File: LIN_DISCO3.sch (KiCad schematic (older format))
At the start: 18 parts, among them J1 Conn_01x06_Female, U1 PIC16F628-xxISO, U2 MCP1804x-5002xMB, U3 Si9243A

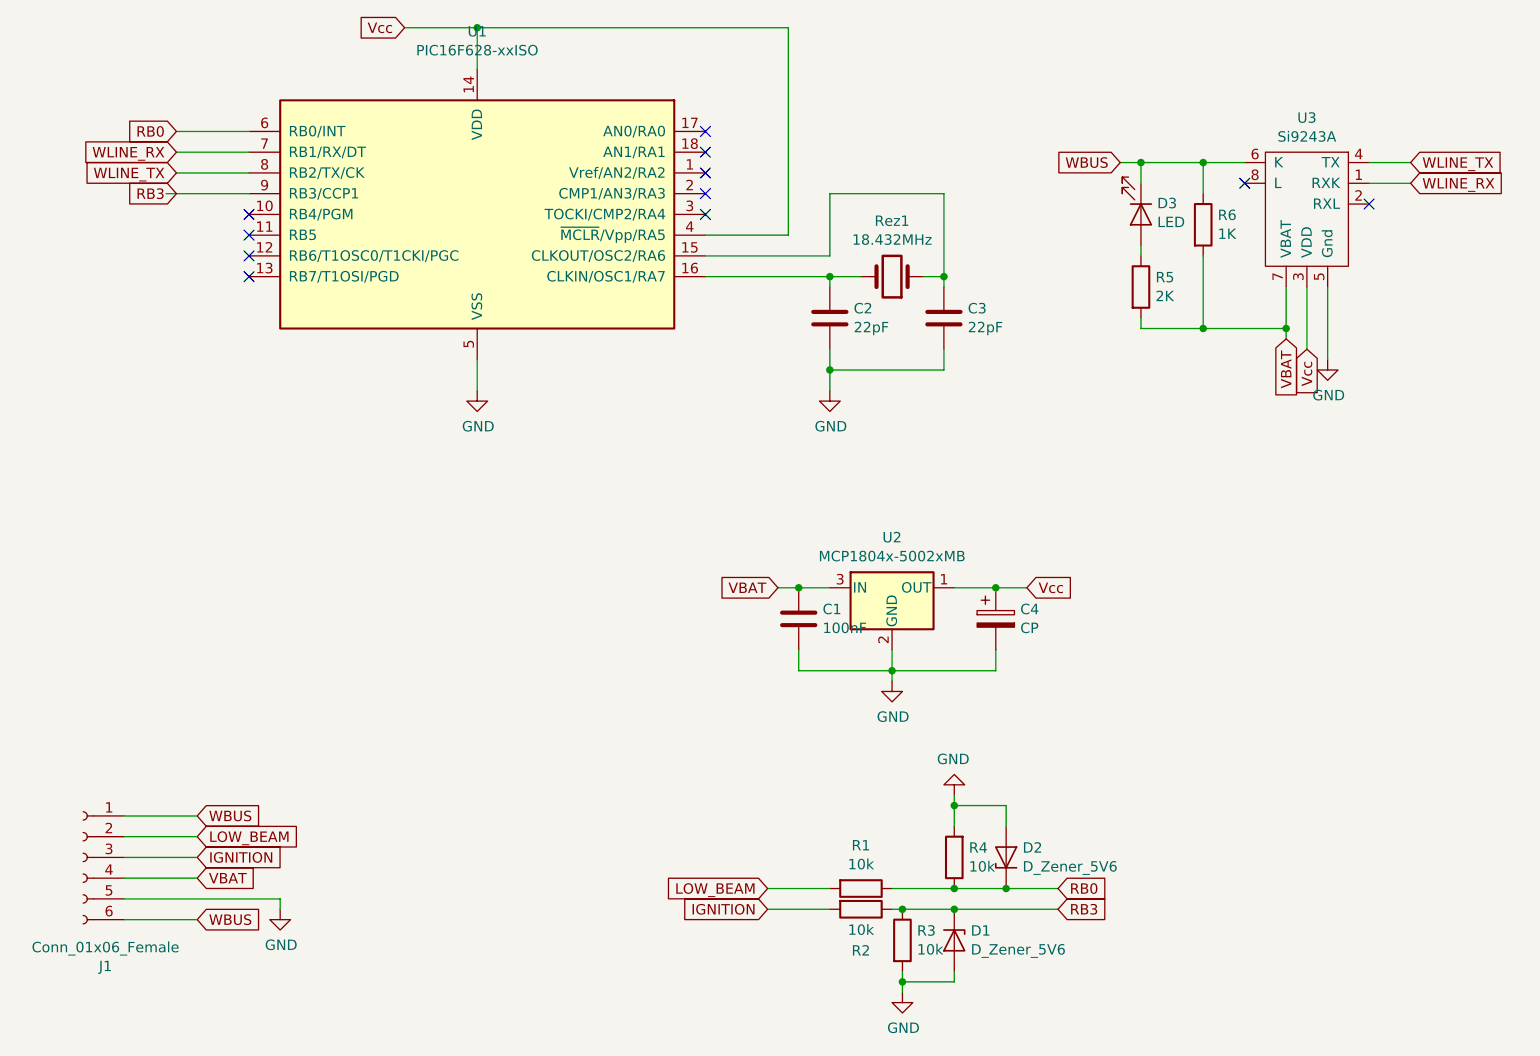
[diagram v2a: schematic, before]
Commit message: added ICSP port
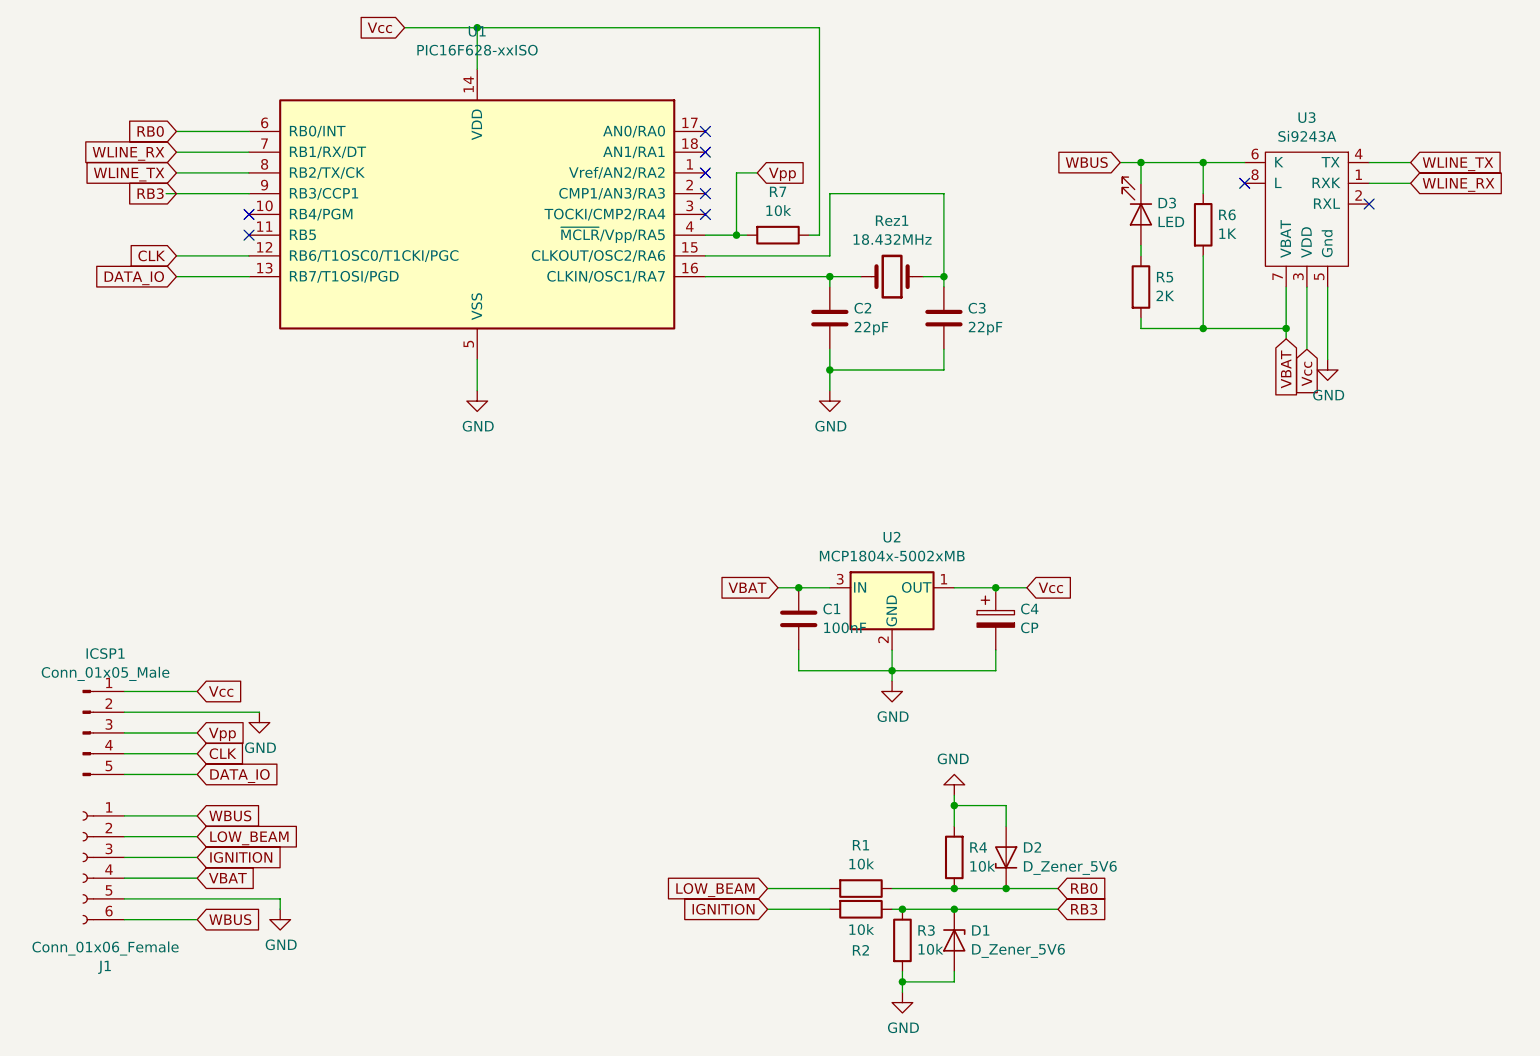
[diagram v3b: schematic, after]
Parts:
- added ICSP1: Conn_01x05_Male, Connector_PinHeader_2.54mm:PinHeader_1x05_P2.54mm_Vertical, symbol Connector:Conn_01x05_Male
- added R7: 10k, Resistor_SMD:R_0805_2012Metric_Pad1.15x1.40mm_HandSolder, symbol Device:R
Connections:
- net GND: now also ICSP1.2 (Pin_2)
- net Vcc: now also ICSP1.1 (Pin_1), R7.1; no longer U1.4 (~MCLR~/Vpp/RA5)
- net CLK: now reaches U1.12 (RB6/T1OSC0/T1CKI/PGC)
- net CLK: now also ICSP1.4 (Pin_4)
- net DATA_IO: now reaches U1.13 (RB7/T1OSI/PGD)
- net DATA_IO: now also ICSP1.5 (Pin_5)
- new net Vpp: ICSP1.3 (Pin_3), R7.2, U1.4 (~MCLR~/Vpp/RA5)
- no-connect marks 11 -> 9
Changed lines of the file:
@@
 $EndDescr
-$Comp
-L MCU_Microchip_PIC16:PIC16F628-xxISO U1
-U 1 1 61EDCCDB
-P 2600 2200
-F 0 "U1" H 2600 3081 50  0000 C CNN
-F 1 "PIC16F628-xxISO" H 2600 2990 50  0000 C CNN
-F 2 "Package_SO:SOIC-18W_7.5x11.6mm_P1.27mm" H 2600 2200 50  0001 C CIN
-F 3 "http://ww1.microchip.com/downloads/en/DeviceDoc/40300c.pdf" H 2600 2200 50  0001 C CNN
-	1    2600 2200
-	1    0    0    -1
-$EndComp
 $Comp
 L Device:Crystal Rez1
@@
 	2600 2900 2600 3050
 Wire Wire Line
-	2600 1300 4100 1300
-Wire Wire Line
-	4100 1300 4100 2300
-Wire Wire Line
-	4100 2300 3700 2300
+	2600 1300 4250 1300
+Wire Wire Line
+	4250 2300 4200 2300
 Connection ~ 2600 1300
 Text GLabel 1150 1900 0    50   Input ~ 0
@@
 NoConn ~ 1500 2200
 NoConn ~ 1500 2300
-NoConn ~ 1500 2400
-NoConn ~ 1500 2500
 Text GLabel 7100 2050 2    50   Input ~ 0
 WLINE_RX
@@
 Wire Wire Line
 	900  5500 1650 5500
+Text GLabel 1150 2400 0    50   Input ~ 0
+CLK
+Wire Wire Line
+	1150 2400 1500 2400
+Text GLabel 1150 2500 0    50   Input ~ 0
+DATA_IO
+Wire Wire Line
+	1150 2500 1500 2500
+$Comp
+L MCU_Microchip_PIC16:PIC16F628-xxISO U1
+U 1 1 61EDCCDB
+P 2600 2200
+F 0 "U1" H 2600 3081 50  0000 C CNN
+F 1 "PIC16F628-xxISO" H 2600 2990 50  0000 C CNN
+F 2 "Package_SO:SOIC-18W_7.5x11.6mm_P1.27mm" H 2600 2200 50  0001 C CIN
+F 3 "http://ww1.microchip.com/downloads/en/DeviceDoc/40300c.pdf" H 2600 2200 50  0001 C CNN
+	1    2600 2200
+	1    0    0    -1
+$EndComp
+Text GLabel 3950 2000 2    50   Input ~ 0
+Vpp
+$Comp
+L Connector:Conn_01x05_Male ICSP1
+U 1 1 61FBFCDB
+P 700 4700
+F 0 "ICSP1" H 808 5081 50  0000 C CNN
+F 1 "Conn_01x05_Male" H 808 4990 50  0000 C CNN
+F 2 "Connector_PinHeader_2.54mm:PinHeader_1x05_P2.54mm_Vertical" H 700 4700 50  0001 C CNN
+F 3 "~" H 700 4700 50  0001 C CNN
+	1    700  4700
+	1    0    0    -1
+$EndComp
+Text GLabel 1250 4500 2    50   Input ~ 0
+Vcc
+$Comp
+L power:GND #PWR0108
+U 1 1 61FC163B
+P 1550 4600
+F 0 "#PWR0108" H 1550 4350 50  0001 C CNN
+F 1 "GND" H 1555 4427 50  0000 C CNN
+F 2 "" H 1550 4600 50  0001 C CNN
+F 3 "" H 1550 4600 50  0001 C CNN
+	1    1550 4600
+	1    0    0    -1
+$EndComp
+Wire Wire Line
+	900  4500 1250 4500
+Wire Wire Line
+	900  4600 1550 4600
+Text GLabel 1250 4700 2    50   Input ~ 0
+Vpp
+Wire Wire Line
+	1250 4700 900  4700
+Text GLabel 1250 4800 2    50   Input ~ 0
+CLK
+Text GLabel 1250 4900 2    50   Input ~ 0
+DATA_IO
+Wire Wire Line
+	1250 4800 900  4800
+Wire Wire Line
+	900  4900 1250 4900
+$Comp
+L Device:R R7
+U 1 1 61FDA942
+P 4050 2300
+F 0 "R7" V 3843 2300 50  0000 C CNN
+F 1 "10k" V 3934 2300 50  0000 C CNN
+F 2 "Resistor_SMD:R_0805_2012Metric_Pad1.15x1.40mm_HandSolder" V 3980 2300 50  0001 C CNN
+F 3 "~" H 4050 2300 50  0001 C CNN
+	1    4050 2300
+	0    1    1    0
+$EndComp
+Wire Wire Line
+	3900 2300 3850 2300
+Wire Wire Line
+	4250 1300 4250 2300
+Wire Wire Line
+	3950 2000 3850 2000
+Wire Wire Line
+	3850 2000 3850 2300
+Connection ~ 3850 2300
+Wire Wire Line
+	3850 2300 3700 2300
 $EndSCHEMATC

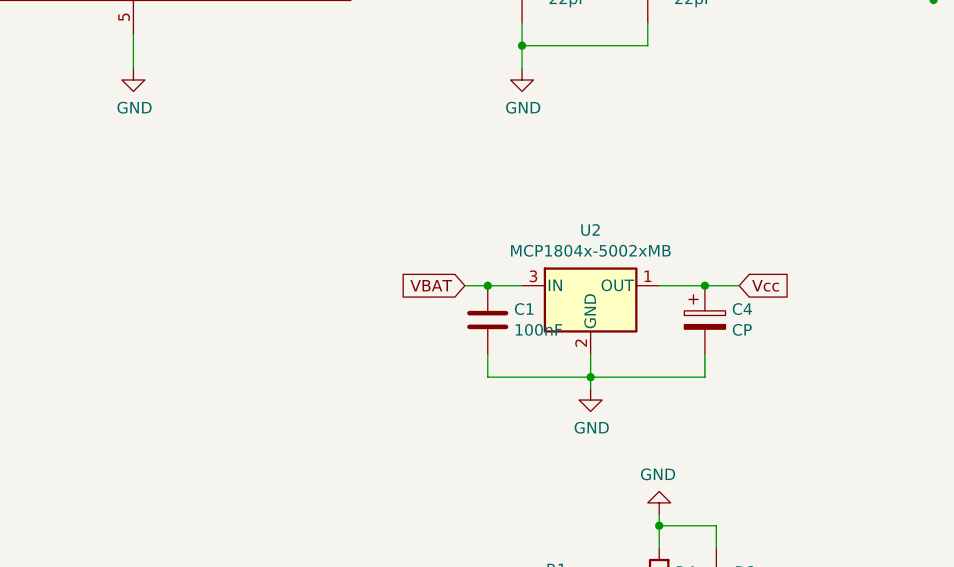
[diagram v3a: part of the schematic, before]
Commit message: design: update conn added fuse power diode bigger cappacitor
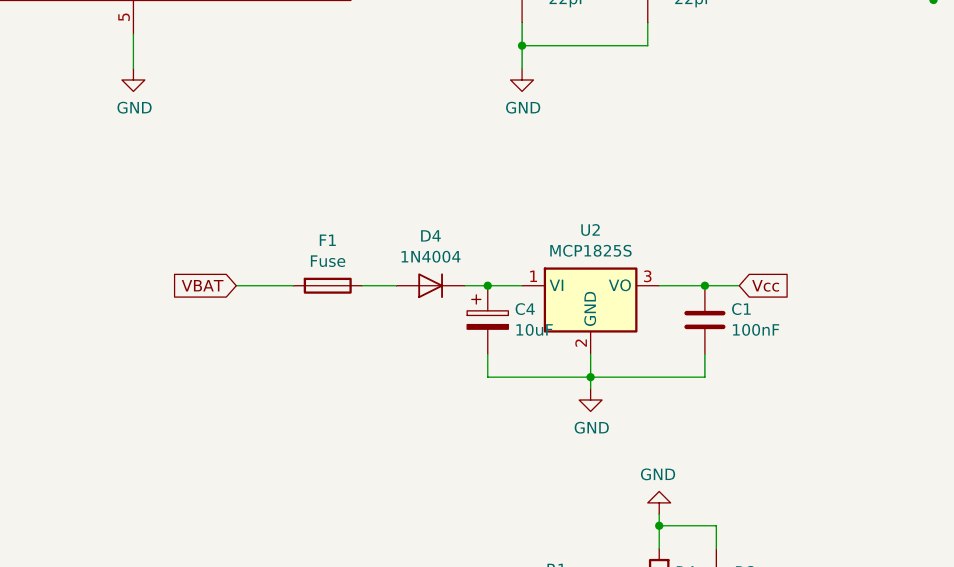
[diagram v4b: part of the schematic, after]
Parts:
- removed U2: MCP1804x-5002xMB, Package_TO_SOT_SMD:SOT-89-3, symbol Regulator_Linear:MCP1804x-5002xMB
- added D4: 1N4004, Diode_SMD:D_SMB, symbol Diode:1N4004
- added F1: Fuse, Fuse:Fuseholder_Cylinder-5x20mm_Stelvio-Kontek_PTF78_Horizontal_Open, symbol Device:Fuse
- added U2: MCP1825S, Package_TO_SOT_SMD:SOT-223-3_TabPin2, symbol Regulator_Linear:MCP1825S
- C4: value CP -> 10uF
- D1, D2: footprint Diode_SMD:D_0805_2012Metric_Pad1.15x1.40mm_HandSolder -> Diode_SMD:D_MiniMELF
- J1: footprint TerminalBlock_4Ucon:TerminalBlock_4Ucon_1x06_P3.50mm_Horizontal -> TerminalBlock_Phoenix:TerminalBlock_Phoenix_PT-1,5-6-5.0-H_1x06_P5.00mm_Horizontal
- Rez1: footprint Crystal:Crystal_SMD_0603-2Pin_6.0x3.5mm_HandSoldering -> Crystal:Crystal_HC49-U_Vertical
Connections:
- net GND: now also U2.2 (GND)
- net VBAT: now also F1.2; no longer C1.1
- net Vcc: now also C1.1, U2.3 (VO); no longer C4.1
- new net: C4.1, D4.1 (K), U2.1 (VI)
- new net: D4.2 (A), F1.1
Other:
- moved on the sheet: C1, C4
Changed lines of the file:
@@
 F 0 "Rez1" H 4600 2232 50  0000 C CNN
 F 1 "18.432MHz" H 4600 2323 50  0000 C CNN
-F 2 "Crystal:Crystal_SMD_0603-2Pin_6.0x3.5mm_HandSoldering" H 4600 2500 50  0001 C CNN
+F 2 "Crystal:Crystal_HC49-U_Vertical" H 4600 2500 50  0001 C CNN
 F 3 "~" H 4600 2500 50  0001 C CNN
 	1    4600 2500
@@
 F 0 "D2" V 5196 5221 50  0000 R CNN
 F 1 "D_Zener_5V6" V 5105 5221 50  0000 R CNN
-F 2 "Diode_SMD:D_0805_2012Metric_Pad1.15x1.40mm_HandSolder" H 5150 5300 50  0001 C CNN
+F 2 "Diode_SMD:D_MiniMELF" H 5150 5300 50  0001 C CNN
 F 3 "~" H 5150 5300 50  0001 C CNN
 	1    5150 5300
@@
 F 0 "D1" V 4854 5779 50  0000 L CNN
 F 1 "D_Zener_5V6" V 4945 5779 50  0000 L CNN
-F 2 "Diode_SMD:D_0805_2012Metric_Pad1.15x1.40mm_HandSolder" H 4900 5700 50  0001 C CNN
+F 2 "Diode_SMD:D_MiniMELF" H 4900 5700 50  0001 C CNN
 F 3 "~" H 4900 5700 50  0001 C CNN
 	1    4900 5700
@@
 	4000 5550 4300 5550
 $Comp
-L Regulator_Linear:MCP1804x-5002xMB U2
-U 1 1 61F18390
-P 4600 4000
-F 0 "U2" H 4600 4242 50  0000 C CNN
-F 1 "MCP1804x-5002xMB" H 4600 4151 50  0000 C CNN
-F 2 "Package_TO_SOT_SMD:SOT-89-3" H 4600 4200 50  0001 C CIN
-F 3 "http://ww1.microchip.com/downloads/en/DeviceDoc/20002200D.pdf" H 4600 3950 50  0001 C CNN
-	1    4600 4000
-	1    0    0    -1
-$EndComp
-$Comp
 L power:GND #PWR0106
 U 1 1 61F18E84
@@
 Wire Wire Line
 	4900 4000 5100 4000
-Text GLabel 4050 4000 0    50   Input ~ 0
+Text GLabel 3050 4000 0    50   Input ~ 0
 VBAT
 Wire Wire Line
@@
 L Device:C C1
 U 1 1 61F1C0DC
+P 5100 4150
+F 0 "C1" H 5215 4196 50  0000 L CNN
+F 1 "100nF" H 5215 4105 50  0000 L CNN
+F 2 "Capacitor_SMD:C_0805_2012Metric_Pad1.15x1.40mm_HandSolder" H 5138 4000 50  0001 C CNN
+F 3 "~" H 5100 4150 50  0001 C CNN
+	1    5100 4150
+	1    0    0    -1
+$EndComp
+Connection ~ 4150 4000
+Wire Wire Line
+	4150 4000 4300 4000
+Wire Wire Line
+	4150 4300 4150 4400
+Wire Wire Line
+	4150 4400 4600 4400
+Connection ~ 4600 4400
+Wire Wire Line
+	4600 4400 4600 4300
+$Comp
+L Device:CP C4
+U 1 1 61F1DF03
 P 4150 4150
-F 0 "C1" H 4265 4196 50  0000 L CNN
-F 1 "100nF" H 4265 4105 50  0000 L CNN
-F 2 "Capacitor_SMD:C_0805_2012Metric_Pad1.15x1.40mm_HandSolder" H 4188 4000 50  0001 C CNN
+F 0 "C4" H 4268 4196 50  0000 L CNN
+F 1 "10uF" H 4268 4105 50  0000 L CNN
+F 2 "Capacitor_SMD:CP_Elec_4x5.8" H 4188 4000 50  0001 C CNN
 F 3 "~" H 4150 4150 50  0001 C CNN
 	1    4150 4150
-	1    0    0    -1
-$EndComp
-Connection ~ 4150 4000
-Wire Wire Line
-	4150 4000 4300 4000
-Wire Wire Line
-	4150 4300 4150 4400
-Wire Wire Line
-	4150 4400 4600 4400
-Connection ~ 4600 4400
-Wire Wire Line
-	4600 4400 4600 4300
-$Comp
-L Device:CP C4
-U 1 1 61F1DF03
-P 5100 4150
-F 0 "C4" H 5218 4196 50  0000 L CNN
-F 1 "CP" H 5218 4105 50  0000 L CNN
-F 2 "Capacitor_SMD:CP_Elec_4x5.8" H 5138 4000 50  0001 C CNN
-F 3 "~" H 5100 4150 50  0001 C CNN
-	1    5100 4150
 	1    0    0    -1
 $EndComp
@@
 F 0 "J1" H 592 4775 50  0000 C CNN
 F 1 "Conn_01x06_Female" H 592 4866 50  0000 C CNN
-F 2 "TerminalBlock_4Ucon:TerminalBlock_4Ucon_1x06_P3.50mm_Horizontal" H 700 5300 50  0001 C CNN
+F 2 "TerminalBlock_Phoenix:TerminalBlock_Phoenix_PT-1,5-6-5.0-H_1x06_P5.00mm_Horizontal" H 700 5300 50  0001 C CNN
 F 3 "~" H 700 5300 50  0001 C CNN
 	1    700  5300
@@
 Wire Wire Line
 	3850 2300 3700 2300
+$Comp
+L Regulator_Linear:MCP1825S U2
+U 1 1 6227C6FC
+P 4600 4000
+F 0 "U2" H 4600 4242 50  0000 C CNN
+F 1 "MCP1825S" H 4600 4151 50  0000 C CNN
+F 2 "Package_TO_SOT_SMD:SOT-223-3_TabPin2" H 4500 4150 50  0001 C CNN
+F 3 "http://ww1.microchip.com/downloads/en/devicedoc/22056b.pdf" H 4600 4250 50  0001 C CNN
+	1    4600 4000
+	1    0    0    -1
+$EndComp
+$Comp
+L Diode:1N4004 D4
+U 1 1 62289964
+P 3900 4000
+F 0 "D4" H 3900 3784 50  0000 C CNN
+F 1 "1N4004" H 3900 3875 50  0000 C CNN
+F 2 "Diode_SMD:D_SMB" H 3900 3825 50  0001 C CNN
+F 3 "http://www.vishay.com/docs/88503/1n4001.pdf" H 3900 4000 50  0001 C CNN
+	1    3900 4000
+	-1   0    0    1
+$EndComp
+Wire Wire Line
+	3600 4000 3750 4000
+$Comp
+L Device:Fuse F1
+U 1 1 6228ED4C
+P 3450 4000
+F 0 "F1" V 3253 4000 50  0000 C CNN
+F 1 "Fuse" V 3344 4000 50  0000 C CNN
+F 2 "Fuse:Fuseholder_Cylinder-5x20mm_Stelvio-Kontek_PTF78_Horizontal_Open" V 3380 4000 50  0001 C CNN
+F 3 "~" H 3450 4000 50  0001 C CNN
+	1    3450 4000
+	0    1    1    0
+$EndComp
+Wire Wire Line
+	3050 4000 3300 4000
 $EndSCHEMATC
